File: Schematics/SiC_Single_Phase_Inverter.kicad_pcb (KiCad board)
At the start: 2 copper layers, 128.5 x 84 mm, 26 parts, among them J1 23AH8785-Black, J2 23AH8786-Red, Q1 STB10NK60ZT4

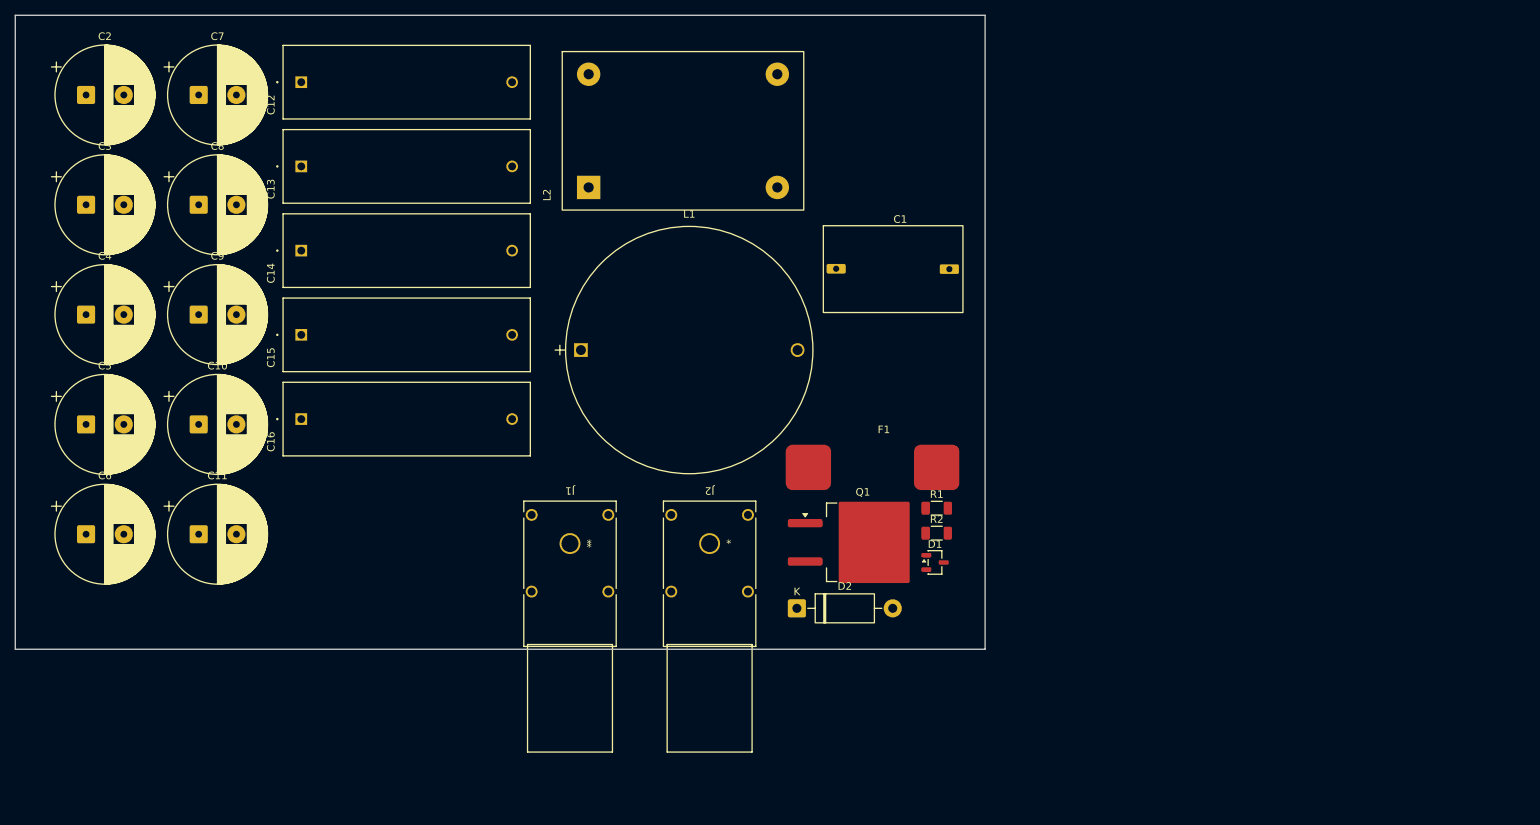
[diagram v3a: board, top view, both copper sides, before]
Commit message: [WIP - SIC Inverter]
- Added 3d models for 3 parts
- Added 3 new footprints for the 3 added parts
- Changed footprint 23AH8785 and 86 Black and Red
- Finished WIP with EMI, Input Protection, and Precharge
- Added datasheet
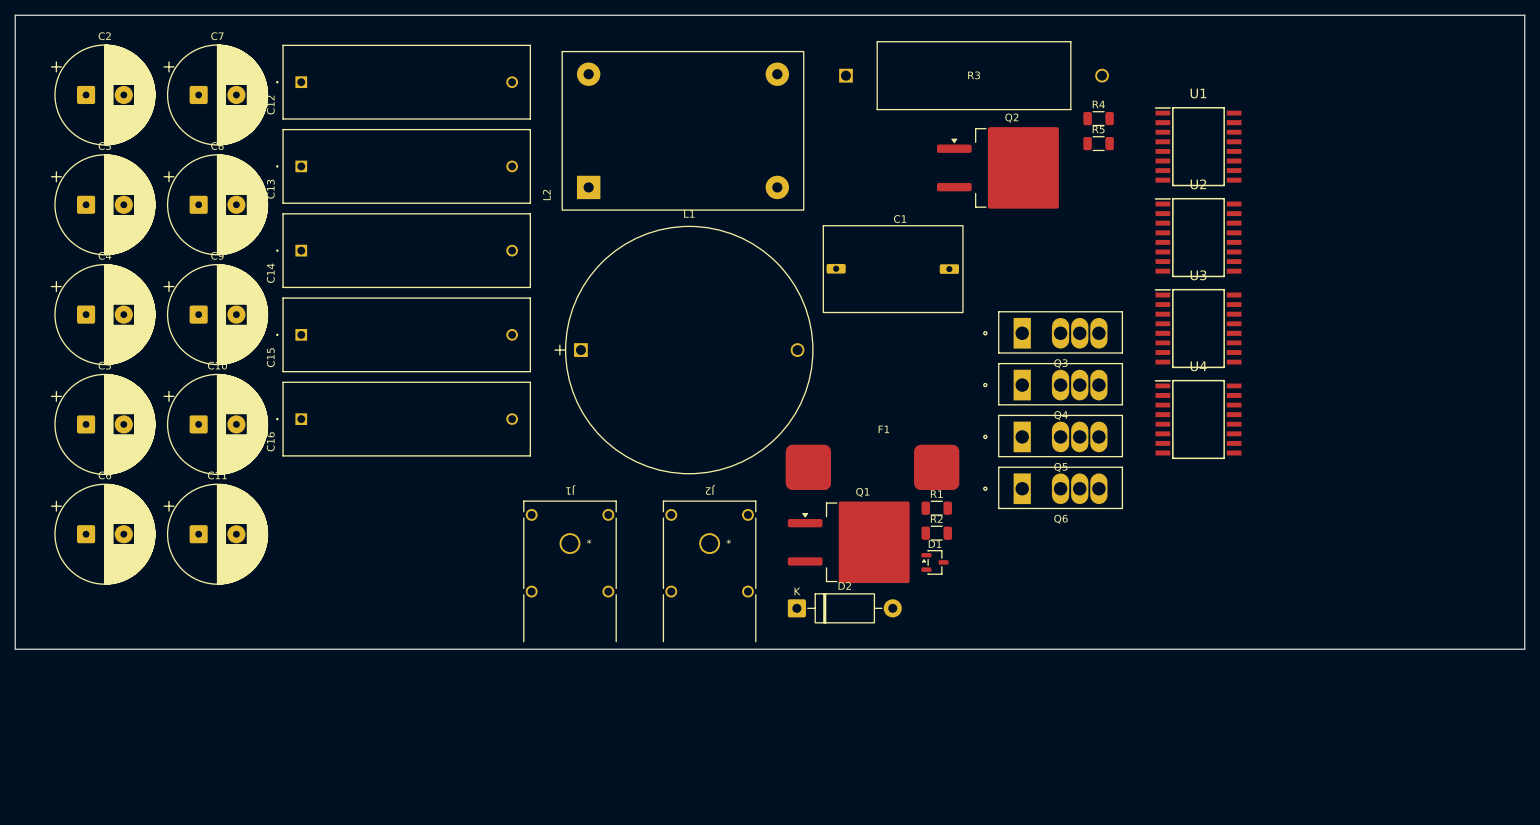
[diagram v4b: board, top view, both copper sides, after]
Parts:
- added Q2: STB10NK60ZT4, Package_TO_SOT_SMD:TO-263-2, F.Cu at (202.1, 57.7)
- added Q3: C3M0025065K, SiC_Inverter:C3M0025065K, F.Cu at (203.4, 79.6)
- added Q4: C3M0025065K, SiC_Inverter:C3M0025065K, F.Cu at (203.4, 86.5)
- added Q5: C3M0025065K, SiC_Inverter:C3M0025065K, F.Cu at (203.4, 93.4)
- added Q6: C3M0025065K, SiC_Inverter:C3M0025065K, F.Cu at (203.4, 100.2)
- added R3: CW005100R0JE12HE, SiC_Inverter:CW005100R0JE12HE, F.Cu at (180.1, 45.5)
- added R4: 47, Resistor_SMD:R_1206_3216Metric, F.Cu at (213.5, 51.2)
- added R5: 100K, Resistor_SMD:R_1206_3216Metric, F.Cu at (213.5, 54.5)
- added U1: UCC21710QDWRQ1, SiC_Inverter:UCC21710QDWRQ1, F.Cu at (226.8, 54.9)
- added U2: UCC21710QDWRQ1, SiC_Inverter:UCC21710QDWRQ1, F.Cu at (226.8, 67.0)
- added U3: UCC21710QDWRQ1, SiC_Inverter:UCC21710QDWRQ1, F.Cu at (226.8, 79.0)
- added U4: UCC21710QDWRQ1, SiC_Inverter:UCC21710QDWRQ1, F.Cu at (226.8, 91.1)
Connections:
- net /DC_Link_Caps/DC+ renamed /DC_Link_Caps/BUS_DC+
- net /Input_Protection/Gate_node renamed /Input_Protection/Gate_node_Inpro
- C10 pad 2: /DC_Link_Caps/DC- -> GND
- C11 pad 2: /DC_Link_Caps/DC- -> GND
- C12 pad 2: /DC_Link_Caps/DC- -> GND
- C13 pad 2: /DC_Link_Caps/DC- -> GND
- C14 pad 2: /DC_Link_Caps/DC- -> GND
- C15 pad 2: /DC_Link_Caps/DC- -> GND
- C16 pad 2: /DC_Link_Caps/DC- -> GND
- C2 pad 2: /DC_Link_Caps/DC- -> GND
- C3 pad 2: /DC_Link_Caps/DC- -> GND
- C4 pad 2: /DC_Link_Caps/DC- -> GND
- C5 pad 2: /DC_Link_Caps/DC- -> GND
- C6 pad 2: /DC_Link_Caps/DC- -> GND
- C7 pad 2: /DC_Link_Caps/DC- -> GND
- C8 pad 2: /DC_Link_Caps/DC- -> GND
- C9 pad 2: /DC_Link_Caps/DC- -> GND
- D2 pad 1: /EMI_Input_Filter/+VIN_EMI -> /Input_Protection/+VIN_Protected
- F1 pad 2: /EMI_Input_Filter/+VIN_EMI -> /Input_Protection/+VIN_Protected
- L2 pad 3: /EMI_Input_Filter/BUS-_Filtered -> GND
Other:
- board size 128.5 x 84 mm -> 200 x 84 mm

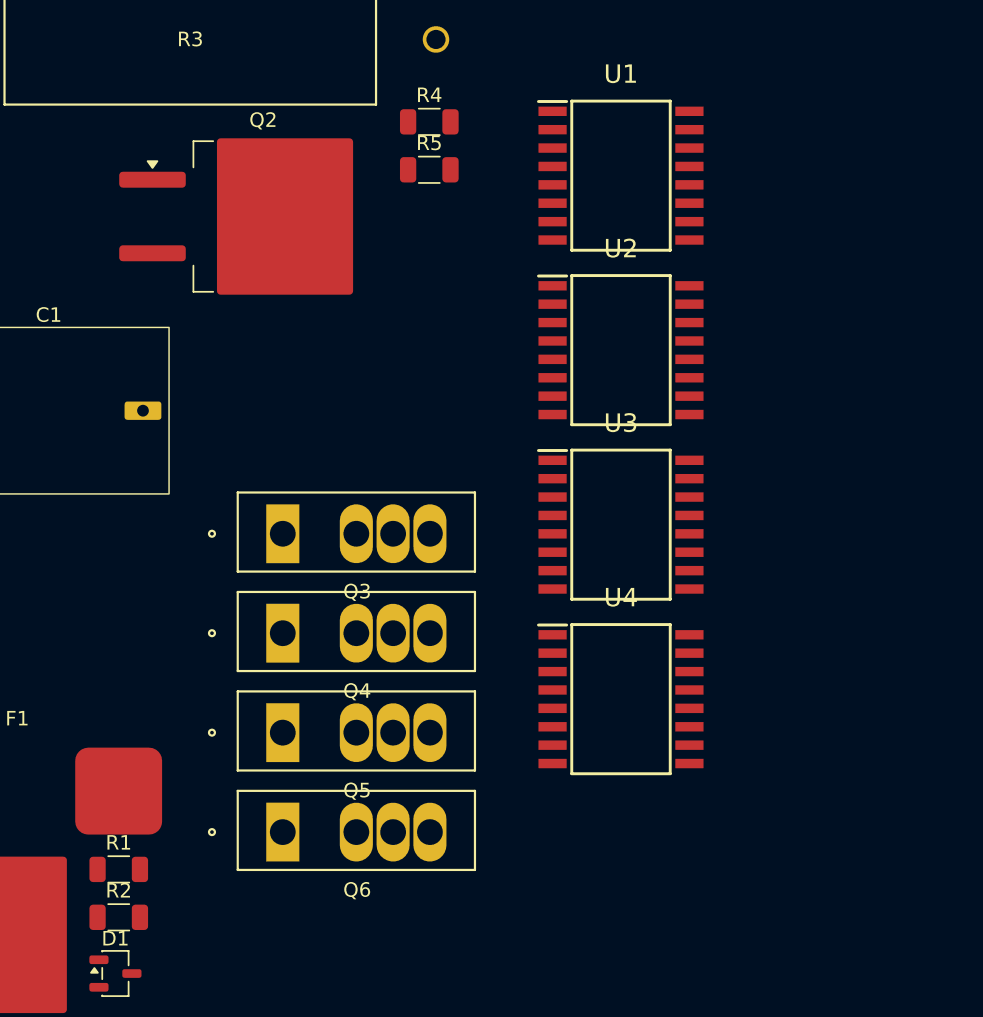
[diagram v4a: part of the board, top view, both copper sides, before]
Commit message: [WIP Full Bridge Leg A High Side]
- Changed Footprint for Black and Red connectors to THP but no Pin
  number
- Changed DC Link cap sub sheet to have a cleaner look
- Change footprint in 1206 reister to head solder pads
- WIP Full Bridge Leg A High Side
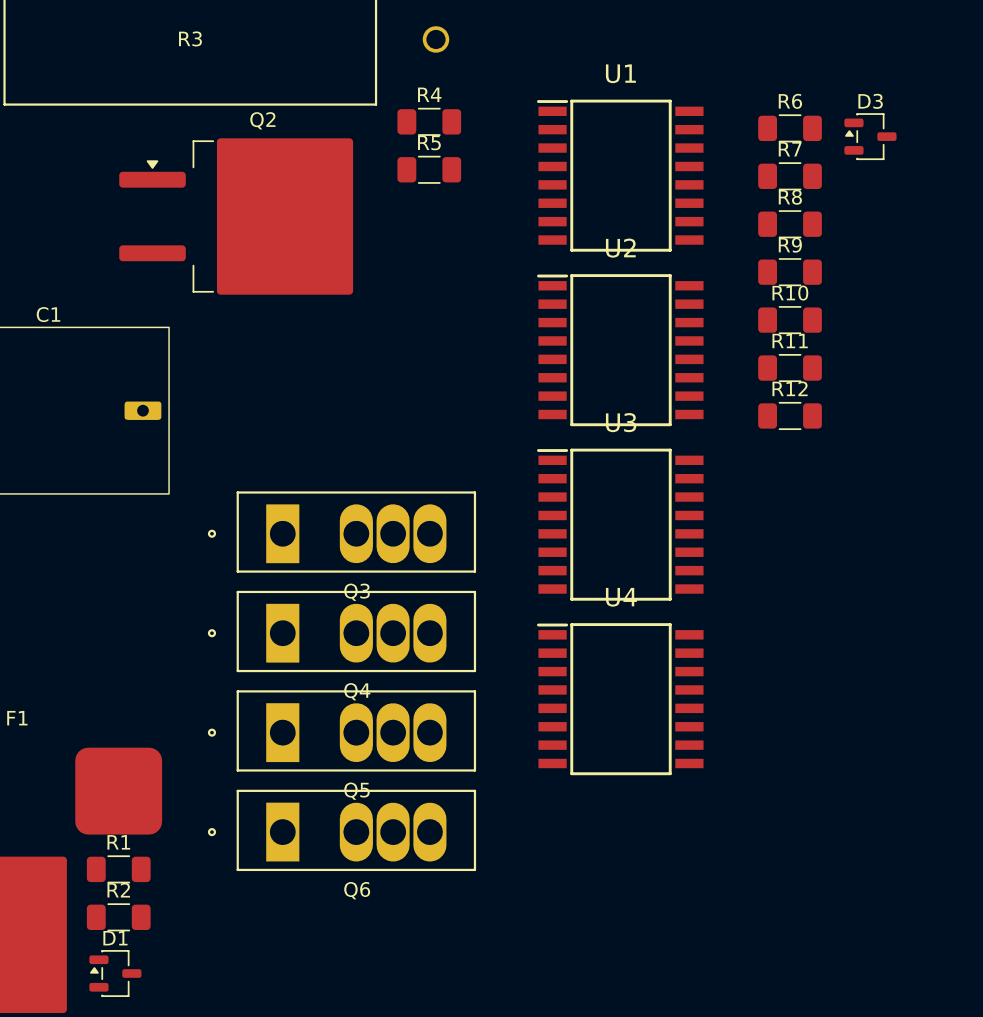
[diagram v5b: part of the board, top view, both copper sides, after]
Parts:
- added D3: BZX84C20-7-F, Package_TO_SOT_SMD:SOT-23-3, F.Cu at (244.0, 52.2)
- added R10: R, Resistor_SMD:R_1206_3216Metric_Pad1.30x1.75mm_HandSolder, F.Cu at (238.4, 64.9)
- added R11: R, Resistor_SMD:R_1206_3216Metric_Pad1.30x1.75mm_HandSolder, F.Cu at (238.4, 68.2)
- added R12: 10K, Resistor_SMD:R_1206_3216Metric_Pad1.30x1.75mm_HandSolder, F.Cu at (238.4, 71.5)
- added R6: 10, Resistor_SMD:R_1206_3216Metric_Pad1.30x1.75mm_HandSolder, F.Cu at (238.4, 51.6)
- added R7: 10, Resistor_SMD:R_1206_3216Metric_Pad1.30x1.75mm_HandSolder, F.Cu at (238.4, 55.0)
- added R8: 100K, Resistor_SMD:R_1206_3216Metric_Pad1.30x1.75mm_HandSolder, F.Cu at (238.4, 58.3)
- added R9: 100, Resistor_SMD:R_1206_3216Metric_Pad1.30x1.75mm_HandSolder, F.Cu at (238.4, 61.6)
- R1, R2, R4, R5: footprint Resistor_SMD:R_1206_3216Metric -> Resistor_SMD:R_1206_3216Metric_Pad1.30x1.75mm_HandSolder
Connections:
- Q3 pad 1: unconnected-(Q3-Pad1) -> /Full-Bridge/BUS_DC+
- Q3 pad 2: unconnected-(Q3-Pad2) -> /Full-Bridge/Phase_A_Node
- Q3 pad 3: unconnected-(Q3-Pad3) -> GND_ISO
- Q3 pad 4: unconnected-(Q3-Pad4) -> /Full-Bridge/LegA_HS_Gate
- Q4 pad 4: unconnected-(Q4-Pad4) -> Net-(Q4-Pad4)
- U1 pad 1: unconnected-(U1-AIN-Pad1) -> GND_ISO
- U1 pad 10: unconnected-(U1-IN+-Pad10) -> Net-(U1-IN+)
- U1 pad 11: unconnected-(U1-IN--Pad11) -> GND
- U1 pad 12: unconnected-(U1-RDY-Pad12) -> /Full-Bridge/HS_LegA_RDY
- U1 pad 13: unconnected-(U1-~{FLT}-Pad13) -> /Full-Bridge/~{HS_LegA_FLT}
- U1 pad 14: unconnected-(U1-~{RST}/EN-Pad14) -> /Full-Bridge/HS_LegA_EN
- U1 pad 15: unconnected-(U1-VCC-Pad15) -> +3V3
- U1 pad 2: unconnected-(U1-OC-Pad2) -> GND_ISO
- U1 pad 3: unconnected-(U1-COM-Pad3) -> GND_ISO
- U1 pad 4: unconnected-(U1-OUTH-Pad4) -> /Full-Bridge/LegA_HS_OUTH
- U1 pad 5: unconnected-(U1-VDD-Pad5) -> +15V_ISO
- U1 pad 6: unconnected-(U1-OUTL-Pad6) -> /Full-Bridge/LegA_HS_OUTL
- U1 pad 7: unconnected-(U1-CLMPI-Pad7) -> /Full-Bridge/LegA_HS_Gate
- U1 pad 8: unconnected-(U1-VEE-Pad8) -> GND_ISO
- U1 pad 9: unconnected-(U1-GND-Pad9) -> GND
- U2 pad 10: unconnected-(U2-IN+-Pad10) -> /Full-Bridge/legA_IN+
- U2 pad 11: unconnected-(U2-IN--Pad11) -> /Full-Bridge/legA_IN-
- U2 pad 13: unconnected-(U2-~{FLT}-Pad13) -> /Full-Bridge/~{LS_LegA_FLT}
- U2 pad 4: unconnected-(U2-OUTH-Pad4) -> Net-(U2-OUTH)
- U2 pad 6: unconnected-(U2-OUTL-Pad6) -> Net-(U2-OUTL)
- U2 pad 9: unconnected-(U2-GND-Pad9) -> GND

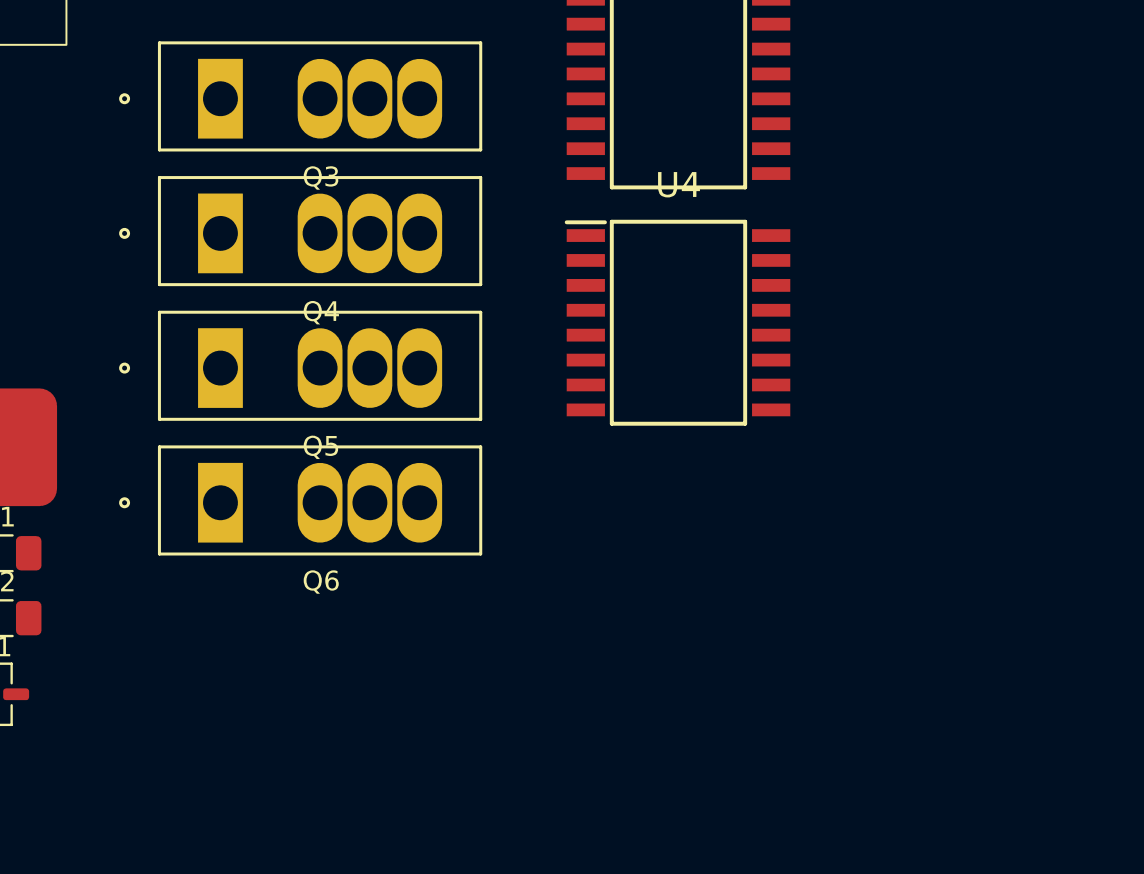
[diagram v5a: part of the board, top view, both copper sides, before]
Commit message: [LEG A WIP]
- moved circuits in Leg A HS and LS
- Completed 90% of HS and LS for LEG A
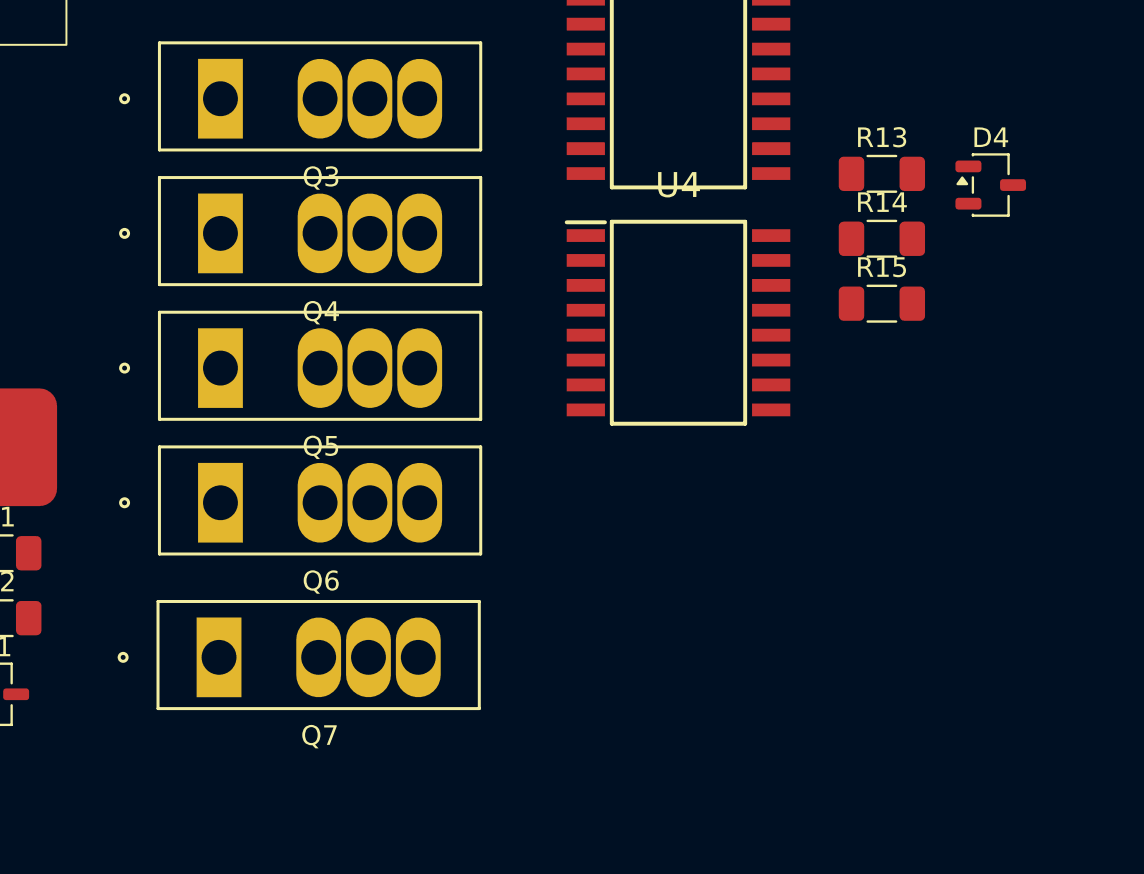
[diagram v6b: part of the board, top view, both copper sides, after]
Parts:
- added D4: BZX84C20-7-F, Package_TO_SOT_SMD:SOT-23-3, F.Cu at (242.7, 84.0)
- added Q7: C3M0025065K, SiC_Inverter:C3M0025065K, F.Cu at (203.3, 108.1)
- added R13: 100K, Resistor_SMD:R_1206_3216Metric_Pad1.30x1.75mm_HandSolder, F.Cu at (237.1, 83.5)
- added R14: 10, Resistor_SMD:R_1206_3216Metric_Pad1.30x1.75mm_HandSolder, F.Cu at (237.1, 86.8)
- added R15: 10, Resistor_SMD:R_1206_3216Metric_Pad1.30x1.75mm_HandSolder, F.Cu at (237.1, 90.1)
- R10: value R -> 10K
- R11: value R -> 100
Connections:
- net +15V_ISO renamed +15V__ISO_LAHS
- net /Full-Bridge/BUS_DC+ renamed /Full-Bridge/Leg_A_Power_Stage/BUS_DC+
- net /Full-Bridge/HS_LegA_EN renamed /Full-Bridge/Leg_A_Power_Stage/HS_LegA_EN
- net /Full-Bridge/HS_LegA_RDY renamed /Full-Bridge/Leg_A_Power_Stage/HS_LegA_RDY
- net /Full-Bridge/LegA_HS_OUTH renamed /Full-Bridge/Leg_A_Power_Stage/LegA_HS_OUTH
- net /Full-Bridge/LegA_HS_OUTL renamed /Full-Bridge/Leg_A_Power_Stage/LegA_HS_OUTL
- net /Full-Bridge/PWM_A_H renamed /Full-Bridge/Leg_A_Power_Stage/PWM_A_H
- net /Full-Bridge/~{HS_LegA_FLT} renamed /Full-Bridge/Leg_A_Power_Stage/~{HS_LegA_FLT}
- net /Full-Bridge/~{LS_LegA_FLT} renamed /Full-Bridge/Leg_A_Power_Stage/~{LS_LegA_FLT}
- D3 pad 1: /Full-Bridge/LegA_HS_Gate -> /Full-Bridge/Leg_A_Power_Stage/LegA_HS_Gate
- D3 pad 2: GND_ISO -> GND_ISO_LAHS
- Q3 pad 2: /Full-Bridge/Phase_A_Node -> GND_ISO_LAHS
- Q3 pad 3: GND_ISO -> GND_ISO_LAHS
- Q3 pad 4: /Full-Bridge/LegA_HS_Gate -> /Full-Bridge/Leg_A_Power_Stage/LegA_HS_Gate
- R10 pad 1: Net-(U2-OUTH) -> /Full-Bridge/Leg_A_Power_Stage/LS_LegA_EN
- R10 pad 2: Net-(Q4-Pad4) -> +3V3
- R11 pad 1: Net-(U2-OUTL) -> Net-(U2-IN+)
- R11 pad 2: Net-(Q4-Pad4) -> /Full-Bridge/Leg_A_Power_Stage/PWM_A_L
- R6 pad 2: /Full-Bridge/LegA_HS_Gate -> /Full-Bridge/Leg_A_Power_Stage/LegA_HS_Gate
- R7 pad 2: /Full-Bridge/LegA_HS_Gate -> /Full-Bridge/Leg_A_Power_Stage/LegA_HS_Gate
- R8 pad 1: /Full-Bridge/LegA_HS_Gate -> /Full-Bridge/Leg_A_Power_Stage/LegA_LS_Gate
- R8 pad 2: GND_ISO -> GND
- U1 pad 1: GND_ISO -> GND_ISO_LAHS
- U1 pad 11: GND -> LOGIC_GND
- U1 pad 2: GND_ISO -> GND_ISO_LAHS
- U1 pad 3: GND_ISO -> GND_ISO_LAHS
- U1 pad 7: /Full-Bridge/LegA_HS_Gate -> /Full-Bridge/Leg_A_Power_Stage/LegA_HS_Gate
- U1 pad 8: GND_ISO -> GND_ISO_LAHS
- U1 pad 9: GND -> LOGIC_GND
- U2 pad 1: unconnected-(U2-AIN-Pad1) -> GND
- U2 pad 10: /Full-Bridge/legA_IN+ -> Net-(U2-IN+)
- U2 pad 11: /Full-Bridge/legA_IN- -> LOGIC_GND
- U2 pad 12: unconnected-(U2-RDY-Pad12) -> /Full-Bridge/Leg_A_Power_Stage/LS_LegA_RDY
- U2 pad 14: unconnected-(U2-~{RST}/EN-Pad14) -> /Full-Bridge/Leg_A_Power_Stage/LS_LegA_EN
- U2 pad 15: unconnected-(U2-VCC-Pad15) -> +3V3
- U2 pad 2: unconnected-(U2-OC-Pad2) -> GND
- U2 pad 3: unconnected-(U2-COM-Pad3) -> GND
- U2 pad 4: Net-(U2-OUTH) -> /Full-Bridge/Leg_A_Power_Stage/LegA_LS_OUTH
- U2 pad 5: unconnected-(U2-VDD-Pad5) -> +15V_LALS
- U2 pad 6: Net-(U2-OUTL) -> /Full-Bridge/Leg_A_Power_Stage/LegA_LS_OUTL
- U2 pad 7: unconnected-(U2-CLMPI-Pad7) -> /Full-Bridge/Leg_A_Power_Stage/LegA_LS_Gate
- U2 pad 8: unconnected-(U2-VEE-Pad8) -> /Full-Bridge/Leg_A_Power_Stage/GND_ISO_LALS
- U2 pad 9: GND -> LOGIC_GND
